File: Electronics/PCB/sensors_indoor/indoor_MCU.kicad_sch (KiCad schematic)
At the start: 12 parts, among them J2 Conn_ST_STDC14, SW1 SW_Push, U1 STM32WBA5MMG, U7 FM24CL16B

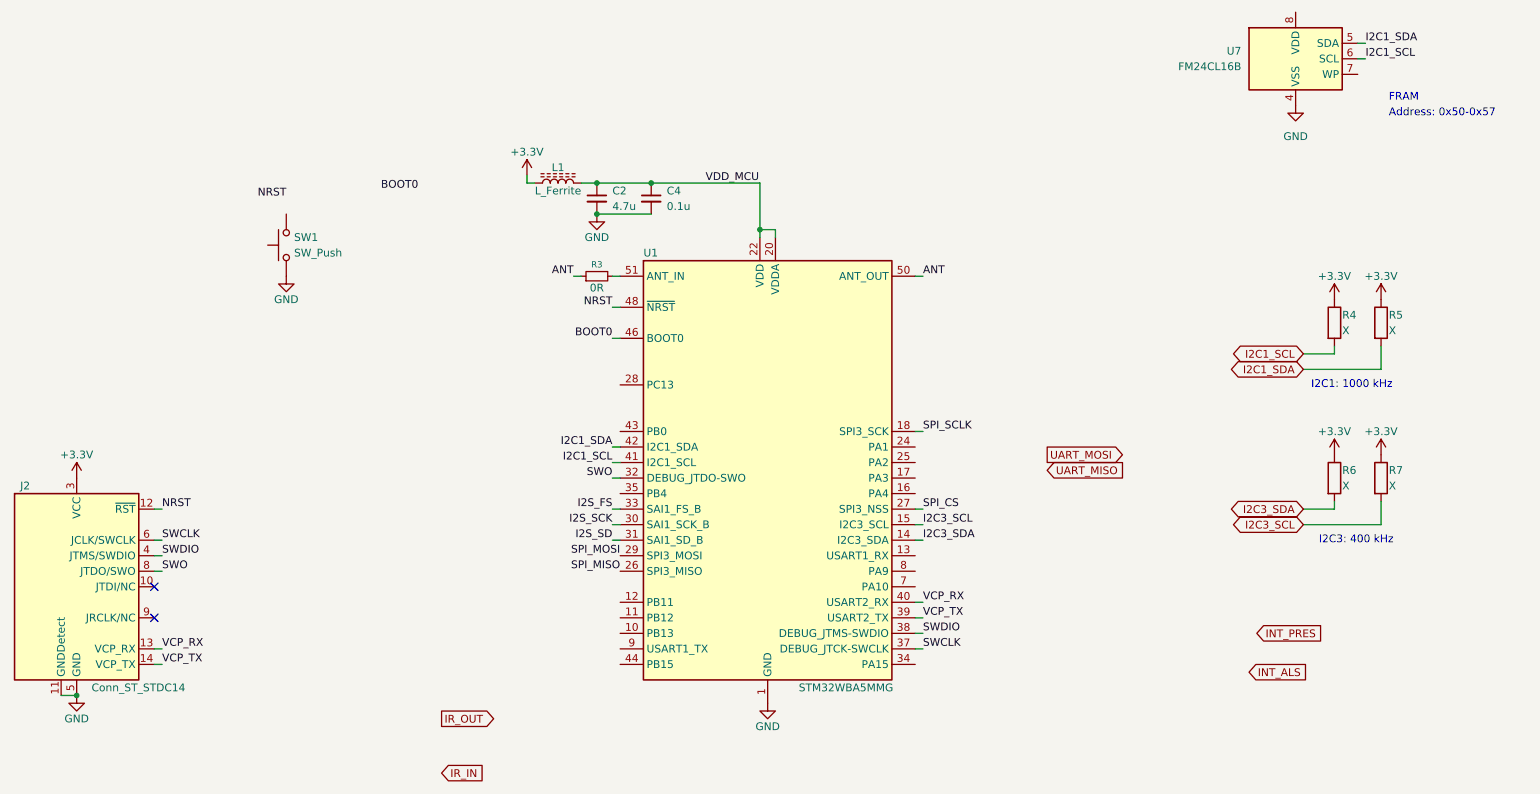
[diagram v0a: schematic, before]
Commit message: Added mounting holes and power supply
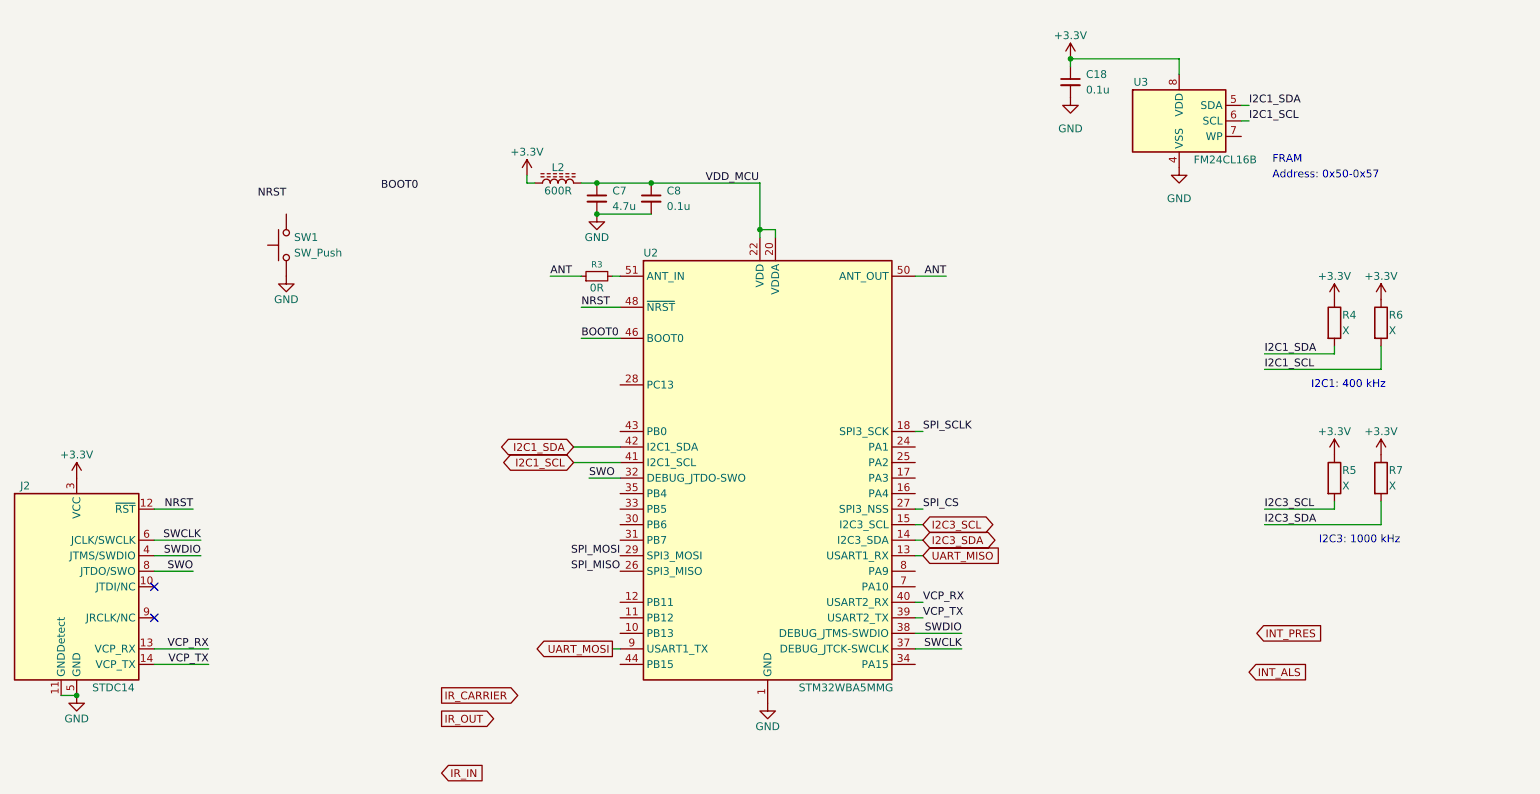
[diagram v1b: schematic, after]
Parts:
- added C18: 0.1u, Capacitor_SMD:C_0402_1005Metric, symbol Device:C_Small
- C7: renamed from C2; footprint (none) -> Capacitor_SMD:C_0805_2012Metric
- C8: renamed from C4; footprint (none) -> Capacitor_SMD:C_0402_1005Metric
- J2: value Conn_ST_STDC14 -> STDC14; footprint Connector_PinHeader_1.27mm:PinHeader_2x07_P1.27mm_Vertical -> ZMPlib:SAMTEC_FTSH-107-01-L-DV-K-A; MPN (none) -> FTSH-107-01-L-DV-K-A; Mouser PN (none) -> 200-FTSH10701LDVKA
- L2: renamed from L1; value L_Ferrite -> 600R; footprint (none) -> Inductor_SMD:L_0805_2012Metric; MPN (none) -> HZ0805E601R-10; Mouser PN (none) -> 875-HZ0805E601R-10
- R4, R7: footprint (none) -> Resistor_SMD:R_0603_1608Metric
- R5: renamed from R6; footprint (none) -> Resistor_SMD:R_0603_1608Metric
- R6: renamed from R5; footprint (none) -> Resistor_SMD:R_0603_1608Metric
- renumbered U1 to U2, U7 to U3
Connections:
- net +3.3V: now also U3.8 (VDD), C18.1
- net GND: now also C18.2; no longer U2.2 (GND), U2.3 (GND), U2.4 (GND), U2.5 (GND), U2.56 (GND), U2.59 (GND)
- net I2C1_SCL: now also R6.2; no longer R4.2
- net I2C1_SDA: now also R4.2; no longer R6.2
- net I2C3_SCL: now also R5.2; no longer R7.2
- net I2C3_SDA: now also R7.2; no longer R5.2
- net UART_MISO: now also U2.13 (PA8)
- net UART_MOSI: now also U2.9 (PB14)
- net I2S_FS: no longer names the net of U2.33 (PB5)
- net I2S_SCK: no longer names the net of U2.30 (PB6)
- net I2S_SD: no longer names the net of U2.31 (PB7)
- new net: U2.2 (GND), U2.3 (GND), U2.4 (GND), U2.5 (GND), U2.56 (GND), U2.59 (GND)
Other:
- note added: "I2C1: 400 kHz"
- note added: "I2C3: 1000 kHz"
- note removed: "I2C1: 1000 kHz"
- note removed: "I2C3: 400 kHz"
- moved on the sheet: U3

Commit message: Swapped sides of everything and started routing
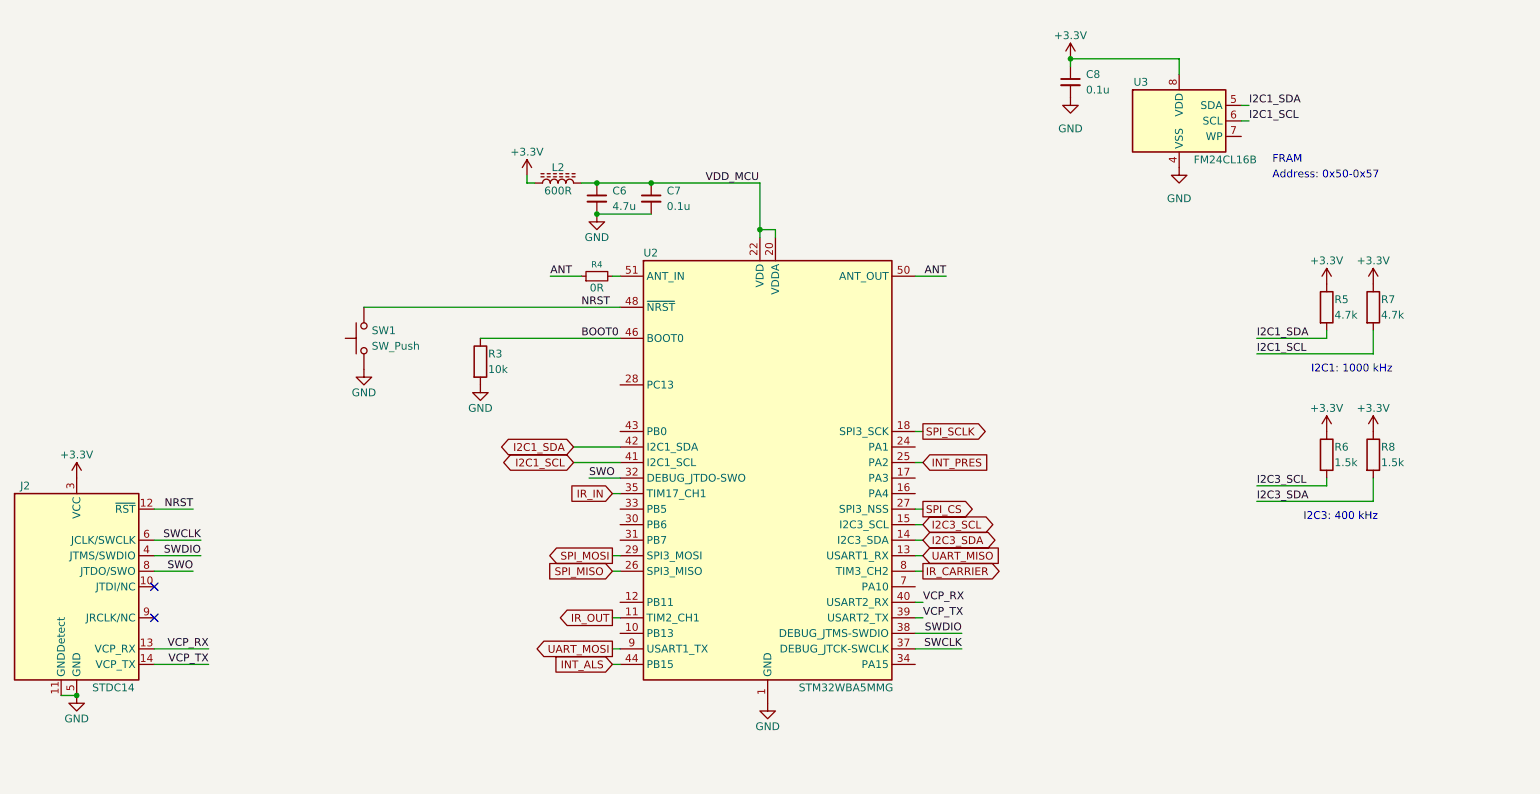
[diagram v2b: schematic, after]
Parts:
- added R3: 10k, Resistor_SMD:R_0603_1608Metric, symbol Device:R
- R5: renamed from R4; value X -> 4.7k
- R6: renamed from R5; value X -> 1.5k
- R7: renamed from R6; value X -> 4.7k
- R8: renamed from R7; value X -> 1.5k
- SW1: footprint (none) -> Button_Switch_THT:SW_PUSH_6mm
- renumbered C7 to C6, C8 to C7, C18 to C8, R3 to R4
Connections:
- net BOOT0: now also R3.1
- net GND: now also R3.2
- net INT_ALS: now also U2.44 (PB15)
- net INT_PRES: now also U2.25 (PA2)
- net IR_CARRIER: now also U2.8 (PA9)
- net IR_IN: now also U2.35 (PB4)
- net IR_OUT: now also U2.11 (PB12)
- net NRST: now also SW1.2
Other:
- note added: "I2C1: 1000 kHz"
- note added: "I2C3: 400 kHz"
- note removed: "I2C1: 400 kHz"
- note removed: "I2C3: 1000 kHz"
- moved on the sheet: R5, R6, R7, R8, SW1

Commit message: Updated PCB with SMD IR tx/rx
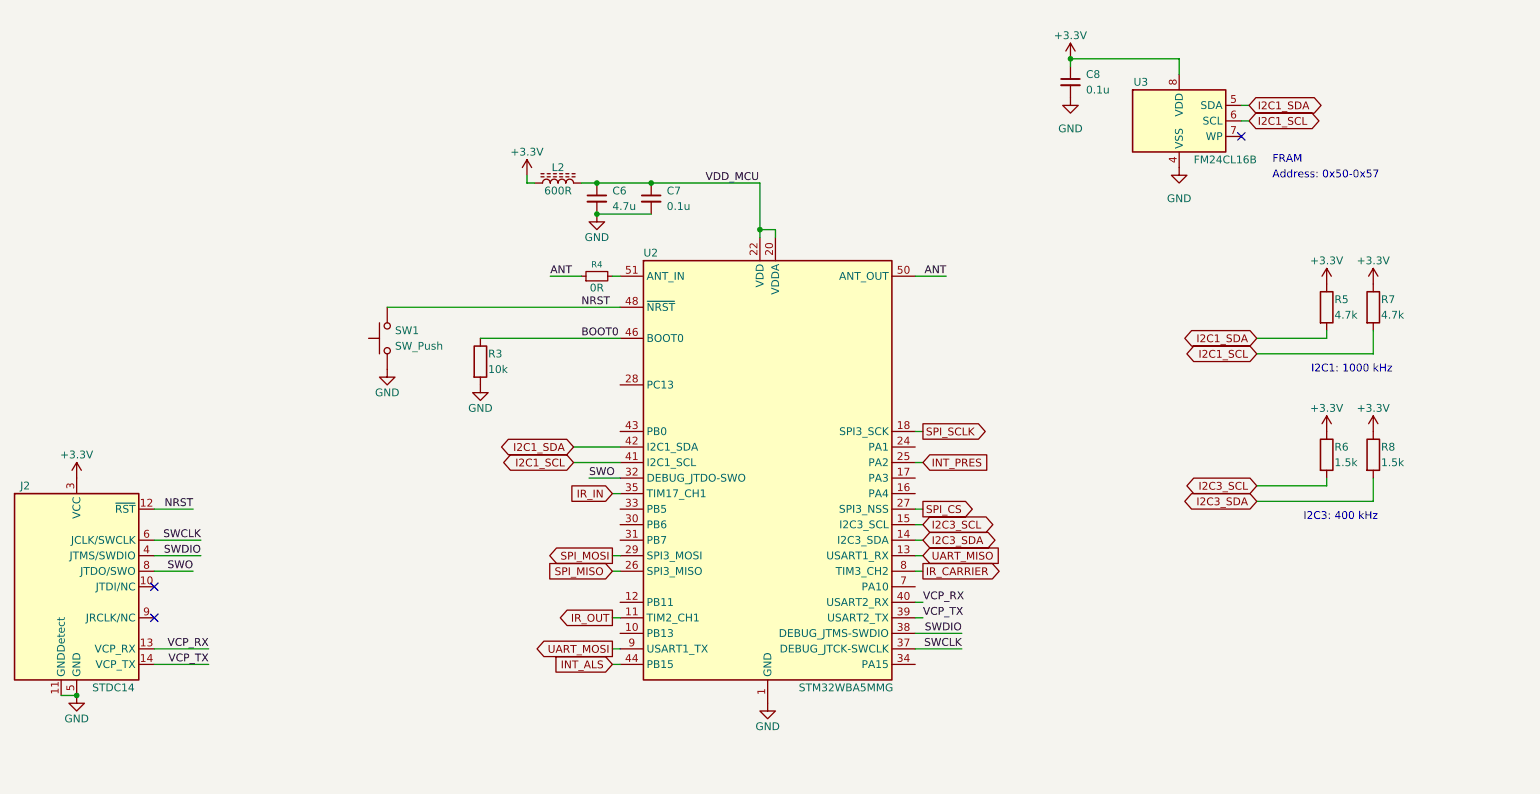
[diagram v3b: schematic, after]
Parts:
- U2: Mouser PN (none) -> 511-STM32WBA5MMGH6TR
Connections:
- no-connect marks 2 -> 3
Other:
- moved on the sheet: SW1
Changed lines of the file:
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@@
+	)
+	(no_connect
+		(at 226.06 38.1)
 	)
 	(no_connect
@@
 	(wire
 		(pts
-			(xy 82.55 66.04) (xy 124.46 66.04)
+			(xy 86.36 66.04) (xy 124.46 66.04)
 		)
 		(stroke
@@
 		)
 	)
-	(label "I2C3_SDA"
-		(at 228.6 97.79 0)
-		(effects
-			(font
-				(size 1.27 1.27)
-			)
-			(justify left bottom)
-		)
-	)
 	(label "SWDIO"
 		(at 55.88 106.68 180)
@@
 		)
 	)
-	(label "I2C1_SDA"
-		(at 227.33 33.02 0)
-		(effects
-			(font
-				(size 1.27 1.27)
-			)
-			(justify left bottom)
-		)
-	)
 	(label "NRST"
 		(at 54.61 99.06 180)
@@
 		)
 	)
-	(label "I2C1_SCL"
-		(at 228.6 73.66 0)
-		(effects
-			(font
-				(size 1.27 1.27)
-			)
-			(justify left bottom)
-		)
-	)
 	(label "SWCLK"
 		(at 55.88 104.14 180)
@@
 		)
 	)
-	(label "I2C3_SCL"
-		(at 228.6 95.25 0)
-		(effects
-			(font
-				(size 1.27 1.27)
-			)
-			(justify left bottom)
-		)
-	)
 	(label "VDD_MCU"
 		(at 138.43 45.72 0)
@@
 		)
 	)
-	(label "I2C1_SCL"
-		(at 227.33 35.56 0)
-		(effects
-			(font
-				(size 1.27 1.27)
-			)
-			(justify left bottom)
-		)
-	)
 	(label "ANT"
 		(at 177.8 60.96 180)
@@
 			)
 			(justify right bottom)
-		)
-	)
-	(label "I2C1_SDA"
-		(at 228.6 71.12 0)
-		(effects
-			(font
-				(size 1.27 1.27)
-			)
-			(justify left bottom)
 		)
 	)
@@
 		)
 	)
+	(global_label "I2C1_SCL"
+		(shape bidirectional)
+		(at 228.6 73.66 180)
+		(fields_autoplaced yes)
+		(effects
+			(font
+				(size 1.27 1.27)
+			)
+			(justify right)
+		)
+		(property "Intersheetrefs" "${INTERSHEET_REFS}"
+			(at 216.8458 73.66 0)
+			(effects
+				(font
+					(size 1.27 1.27)
+				)
+				(justify right)
+			)
+		)
+	)
 	(global_label "SPI_MOSI"
 		(shape output)
@@
 		)
 	)
+	(global_label "I2C1_SCL"
+		(shape bidirectional)
+		(at 227.33 35.56 0)
+		(fields_autoplaced yes)
+		(effects
+			(font
+				(size 1.27 1.27)
+			)
+			(justify left)
+		)
+		(property "Intersheetrefs" "${INTERSHEET_REFS}"
+			(at 239.0842 35.56 0)
+			(effects
+				(font
+					(size 1.27 1.27)
+				)
+				(justify left)
+			)
+		)
+	)
 	(global_label "UART_MISO"
 		(shape input)
@@
 		)
 	)
+	(global_label "I2C1_SDA"
+		(shape bidirectional)
+		(at 227.33 33.02 0)
+		(fields_autoplaced yes)
+		(effects
+			(font
+				(size 1.27 1.27)
+			)
+			(justify left)
+		)
+		(property "Intersheetrefs" "${INTERSHEET_REFS}"
+			(at 239.1447 33.02 0)
+			(effects
+				(font
+					(size 1.27 1.27)
+				)
+				(justify left)
+			)
+		)
+	)
+	(global_label "I2C3_SDA"
+		(shape bidirectional)
+		(at 228.6 97.79 180)
+		(fields_autoplaced yes)
+		(effects
+			(font
+				(size 1.27 1.27)
+			)
+			(justify right)
+		)
+		(property "Intersheetrefs" "${INTERSHEET_REFS}"
+			(at 216.7853 97.79 0)
+			(effects
+				(font
+					(size 1.27 1.27)
+				)
+				(justify right)
+			)
+		)
+	)
 	(global_label "INT_PRES"
 		(shape input)
@@
 		)
 	)
+	(global_label "I2C3_SCL"
+		(shape bidirectional)
+		(at 228.6 95.25 180)
+		(fields_autoplaced yes)
+		(effects
+			(font
+				(size 1.27 1.27)
+			)
+			(justify right)
+		)
+		(property "Intersheetrefs" "${INTERSHEET_REFS}"
+			(at 216.8458 95.25 0)
+			(effects
+				(font
+					(size 1.27 1.27)
+				)
+				(justify right)
+			)
+		)
+	)
 	(global_label "I2C1_SDA"
 		(shape bidirectional)
@@
 		(property "Intersheetrefs" "${INTERSHEET_REFS}"
 			(at 105.0253 88.9 0)
+			(effects
+				(font
+					(size 1.27 1.27)
+				)
+				(justify right)
+			)
+		)
+	)
+	(global_label "I2C1_SDA"
+		(shape bidirectional)
+		(at 228.6 71.12 180)
+		(fields_autoplaced yes)
+		(effects
+			(font
+				(size 1.27 1.27)
+			)
+			(justify right)
+		)
+		(property "Intersheetrefs" "${INTERSHEET_REFS}"
+			(at 216.7853 71.12 0)
 			(effects
 				(font
@@
 	(symbol
 		(lib_id "Switch:SW_Push")
-		(at 82.55 71.12 90)
+		(at 86.36 71.12 90)
 		(unit 1)
 		(exclude_from_sim no)
@@
 		(fields_autoplaced yes)
 		(property "Reference" "SW1"
-			(at 83.82 69.8499 90)
+			(at 87.63 69.8499 90)
 			(effects
 				(font
@@
 		)
 		(property "Value" "SW_Push"
-			(at 83.82 72.3899 90)
+			(at 87.63 72.3899 90)
 			(effects
 				(font
@@
 		)
 		(property "Footprint" "Button_Switch_THT:SW_PUSH_6mm"
-			(at 77.47 71.12 0)
+			(at 81.28 71.12 0)
 			(effects
 				(font
@@
 		)
 		(property "Datasheet" "~"
-			(at 77.47 71.12 0)
+			(at 81.28 71.12 0)
 			(effects
 				(font
@@
 		)
 		(property "Description" "Push button switch, generic, two pins"
-			(at 82.55 71.12 0)
+			(at 86.36 71.12 0)
 			(effects
 				(font
@@
 	(symbol
 		(lib_id "power:GND")
-		(at 82.55 76.2 0)
+		(at 86.36 76.2 0)
 		(unit 1)
 		(exclude_from_sim no)
@@
 		(dnp no)
 		(property "Reference" "#PWR013"
-			(at 82.55 82.55 0)
+			(at 86.36 82.55 0)
 			(effects
 				(font
@@
 		)
 		(property "Value" "GND"
-			(at 82.55 80.01 0)
+			(at 86.36 80.01 0)
 			(effects
 				(font
@@
 		)
 		(property "Footprint" ""
-			(at 82.55 76.2 0)
+			(at 86.36 76.2 0)
 			(effects
 				(font
@@
 		)
 		(property "Datasheet" ""
-			(at 82.55 76.2 0)
+			(at 86.36 76.2 0)
 			(effects
 				(font
@@
 		)
 		(property "Description" "Power symbol creates a global label with name \"GND\" , ground"
-			(at 82.55 76.2 0)
+			(at 86.36 76.2 0)
 			(effects
 				(font
@@
 			)
 		)
-		(property "Mouser PN" ""
+		(property "Mouser PN" "511-STM32WBA5MMGH6TR"
 			(at 148.59 92.71 0)
 			(effects
